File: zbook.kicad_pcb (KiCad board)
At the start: 4 copper layers, 187 parts, among them J1 USB_C_Receptacle_USB2.0_16P, J2 B2B-XH-A, J3 USB_C_Receptacle_USB2.0_16P, J4 Conn_01x03_Pin, J5 Conn_01x05_Pin, J6 Conn_02x04_Odd_Even, J7 Conn_02x15_Counter_Clockwise, J8 MSD-4-A, J9 DISPLAY CONN, Q1 Q_NMOS_GSD, Q2 Q_Photo_NPN, Q3 SL2301S, Q4 T2N7002AK,LM, SW1 SW_SPDT, SW2 SW_Push, SW3 SW_Push, SW4 SW_Push, SW5 SW_Push, SW6 SW_Push, SW7 SW_Push, U3 RP2040, U5 W25Q16JVSS, U6 W25Q16JVSS, U7 GSDA213, Y1 12MHz/10pF, Y2 12MHz/10pF

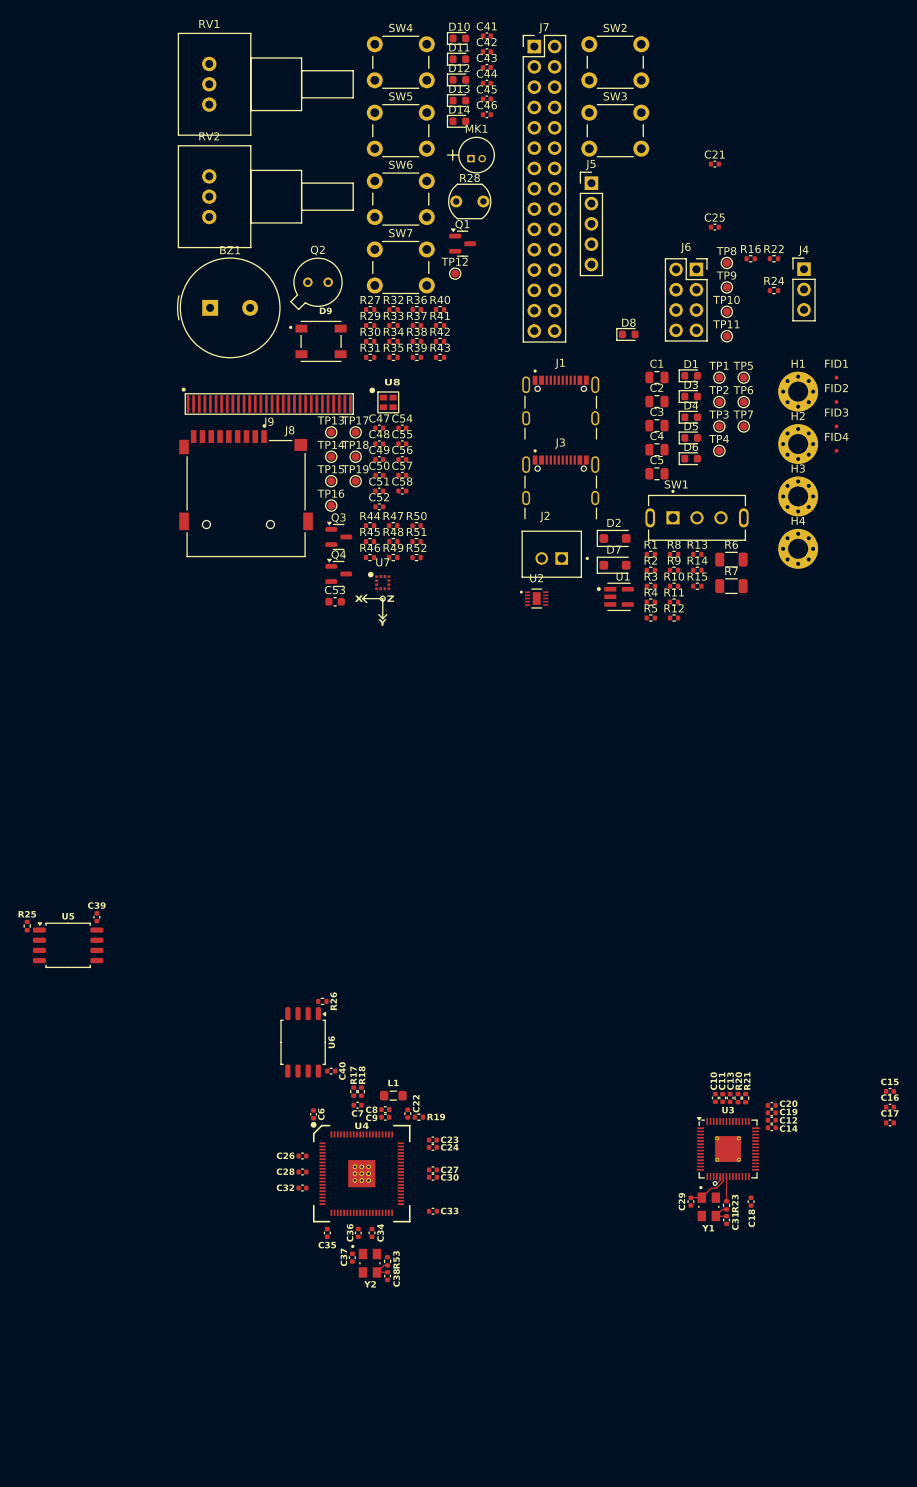
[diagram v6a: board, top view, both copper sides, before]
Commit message: wip: places more rp circuitry
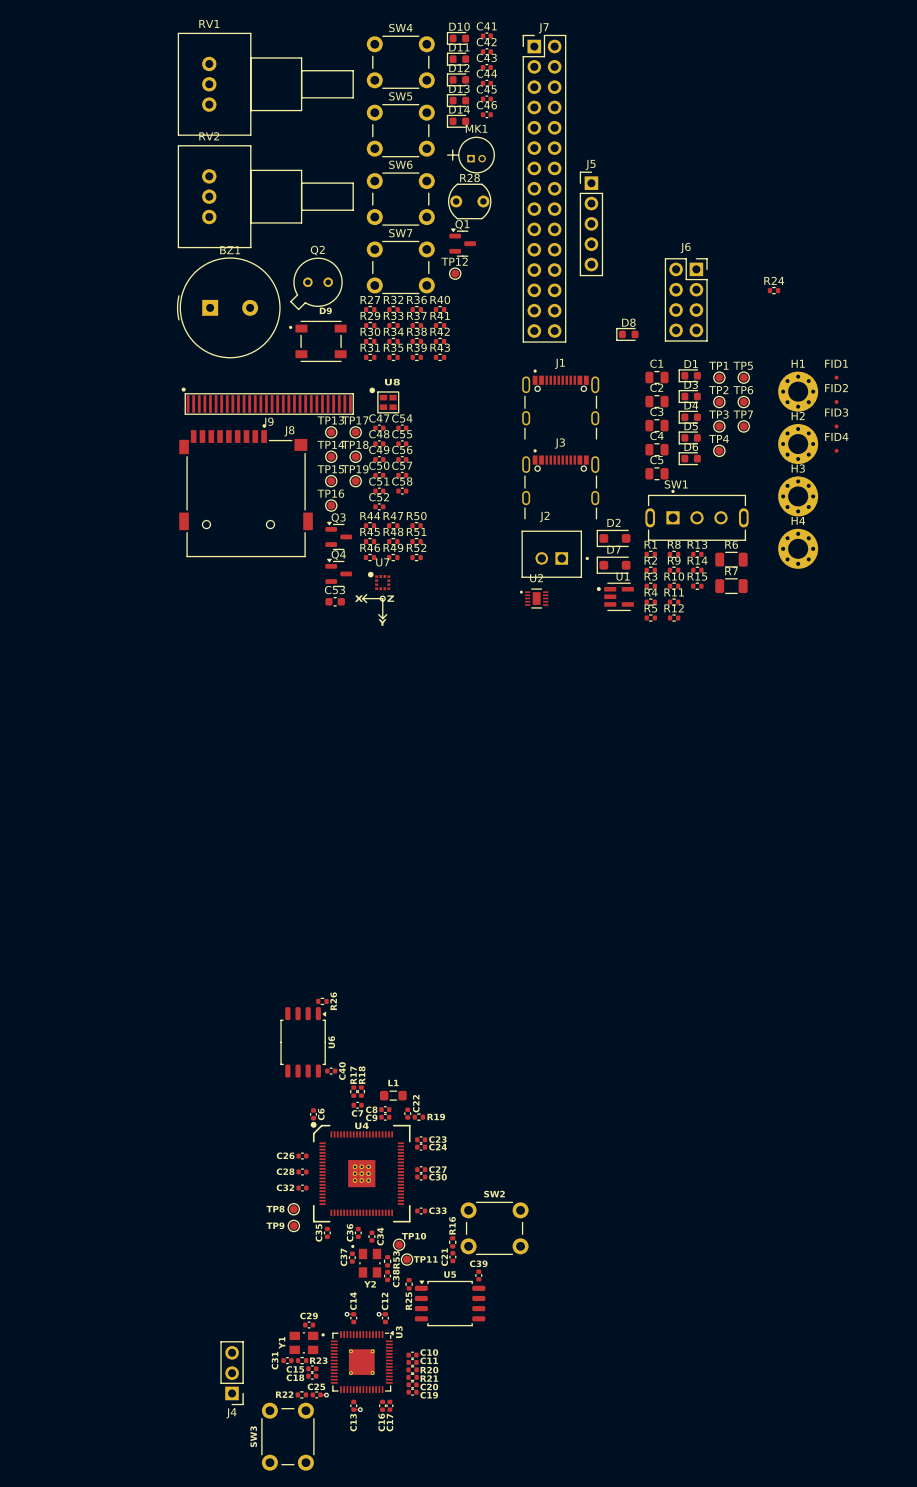
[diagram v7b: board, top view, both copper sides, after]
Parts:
- moved SW3 173.4 mm to (345.4, 236.2), turned to 90 degrees
- moved J4 157.7 mm to (340.6, 227.6), turned to 180 degrees
- moved C25 154.2 mm to (351.2, 227.8)
- moved R22 153.8 mm to (349.4, 227.8), turned to 180 degrees
- moved SW2 146.5 mm to (370.2, 204.7)
- moved C21 140.5 mm to (368.2, 210.5), turned to -90 degrees
- moved TP8 130.1 mm to (348.4, 204.6)
- moved TP9 129.2 mm to (348.4, 206.6)
- moved R16 128.5 mm to (368.2, 208.7), turned to 90 degrees
- moved TP10 123.6 mm to (361.5, 209.0)
- moved TP11 122.1 mm to (362.5, 210.8)
- moved C15 80.1 mm to (350.7, 224.5), turned to 180 degrees
- moved C16 73.6 mm to (359.4, 229.1), turned to -90 degrees
- moved C17 71.8 mm to (360.4, 229.1), turned to -90 degrees
- moved C39 65.5 mm to (371.5, 212.8)
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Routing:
- net Net-(U3-XIN): track 5.49 -> 0.00 mm
- net Net-(U3-XOUT): track 3.10 -> 0.00 mm
- net Net-(C31-Pad1): track 3.03 -> 0.00 mm
- net Net-(C38-Pad1): track 3.03 -> 0.00 mm
- net GND: track 1.28 -> 3.44 mm, vias 1 -> 4
- net +3V3: track 0.55 -> 0.00 mm

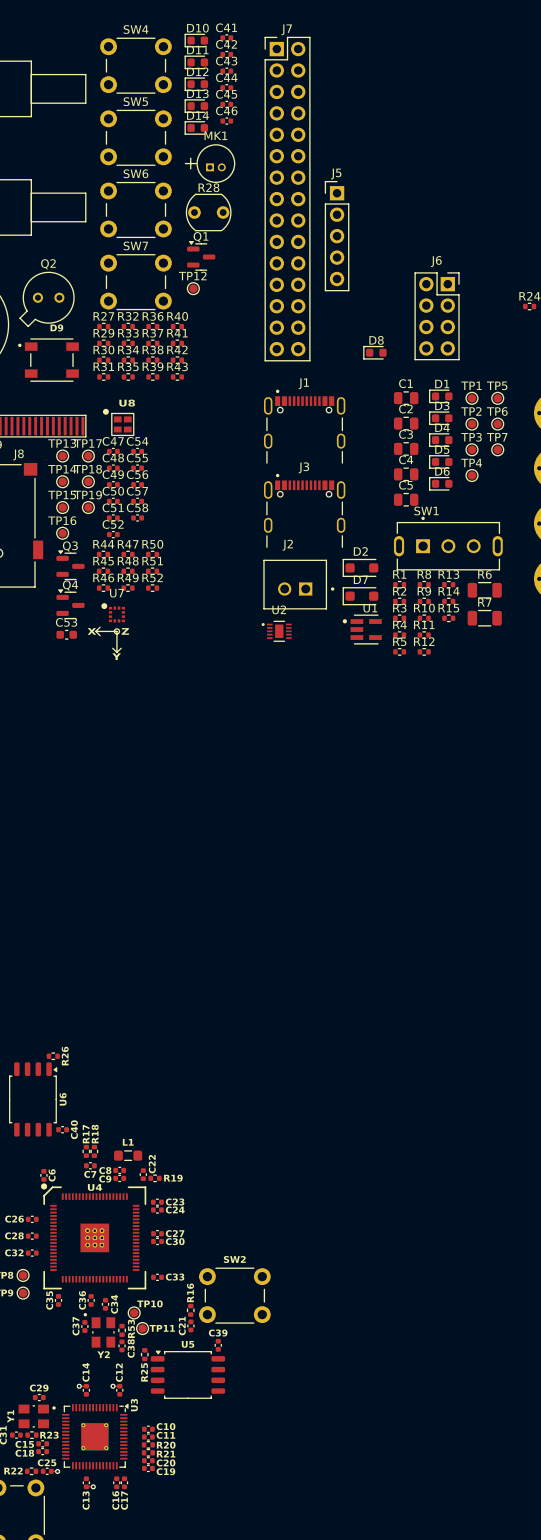
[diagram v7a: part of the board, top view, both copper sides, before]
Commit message: feat: adds pull-up resistors to wi-fi header
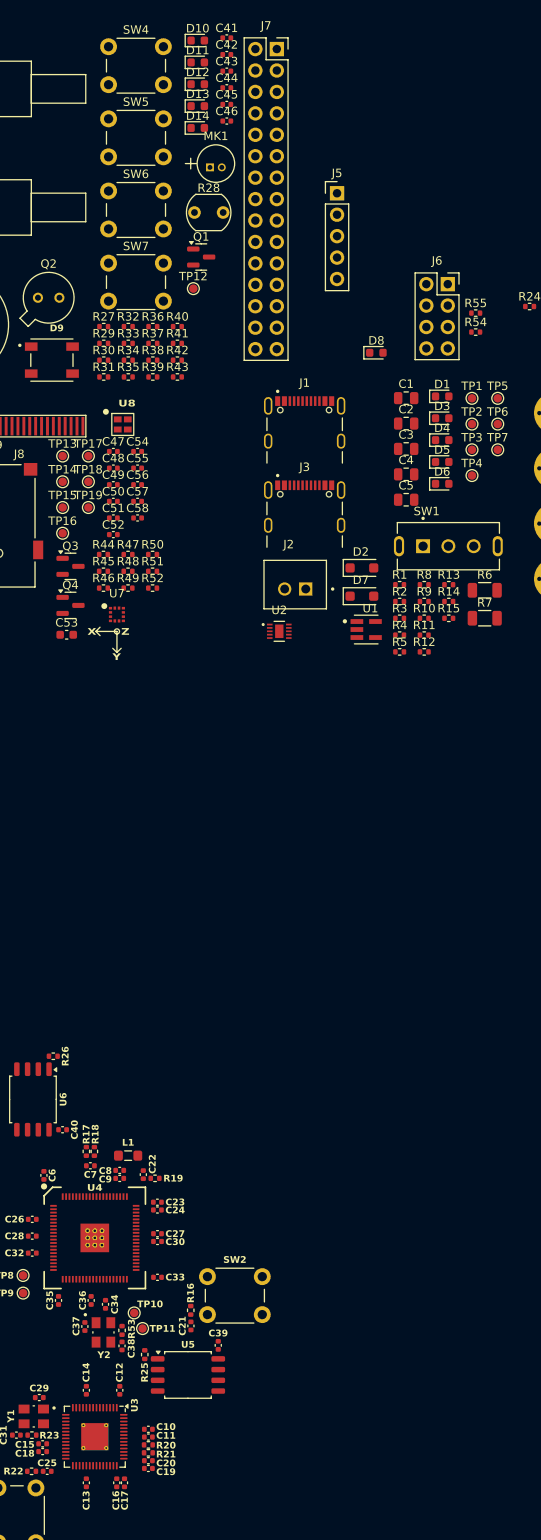
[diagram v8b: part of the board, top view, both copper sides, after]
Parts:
- added R54: 10k, Resistor_SMD:R_0402_1005Metric, F.Cu at (402.0, 92.8)
- added R55: 10k, Resistor_SMD:R_0402_1005Metric, F.Cu at (402.0, 90.5)
- J7: footprint Connector_PinHeader_2.54mm:PinHeader_2x15_P2.54mm_Vertical -> Connector_PinSocket_2.54mm:PinSocket_2x15_P2.54mm_Vertical
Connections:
- J6 pad 3: unconnected-(J6-Pin_3-Pad3) -> Net-(J6-Pin_3)
- J6 pad 5: unconnected-(J6-Pin_5-Pad5) -> Net-(J6-Pin_5)
- J7 pad 16: GND -> /Microcontroller/SWCLK
- J7 pad 17: GND -> /Microcontroller/SWDIO
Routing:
- net GND: track 3.44 -> 0.00 mm, vias 4 -> 0
